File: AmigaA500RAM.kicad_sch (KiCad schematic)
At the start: 0 parts

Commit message: Amiga A500 RAM Schematic
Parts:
- added C1, C2: 1uF, Capacitor_SMD:C_0805_2012Metric, symbol Device:C_Small
- added C10, C11, C12, C13, C14, C3, C4, C5, C6, C7, C8, C9: 0.1uF, Capacitor_SMD:C_0805_2012Metric, symbol Device:C_Small
- added J1: SSQ-128-02-G-D-RA, AmigaA500RAM:PinSocket_2x28_P2.54mm_Horizontal_A501, symbol Connector_Generic:Conn_02x28_Odd_Even
- added JP1: 1MB, Jumper:SolderJumper-2_P1.3mm_Open_RoundedPad1.0x1.5mm, symbol Jumper:SolderJumper_2_Open
- added JP2: CAS 3x or 2x delay, Jumper:SolderJumper-3_P1.3mm_Bridged2Bar12_RoundedPad1.0x1.5mm, symbol Jumper:SolderJumper_3_Bridged12
- added NT1, NT2, NT3, NT4: NetTie_2, NetTie:NetTie-2_SMD_Pad0.5mm, symbol Device:NetTie_2
- added R1, R2, R3: 10K, Resistor_SMD:R_0805_2012Metric, symbol Device:R_Small
- added RN1, RN2, RN3: EXB-2HV680JV, AmigaA500RAM:R_Array08_EXB2H, symbol Device:R_Pack08
- added TP1: TestPoint_Small, AmigaA500RAM:TestPoint_Keystone_5016_Compact, symbol Connector:TestPoint_Small
- added TP2, TP3, TP4, TP5, TP6, TP7: TestPoint_Small, TestPoint:TestPoint_Pad_D1.0mm, symbol Connector:TestPoint_Small
- added U1: 74LVC16T245, Package_SO:TSSOP-48_6.1x12.5mm_P0.5mm, symbol 74xx:74ALVC164245
- added U2: TLV1117LV33, Package_TO_SOT_SMD:SOT-223-3_TabPin2, symbol AmigaA500RAM:TLV1117LV33
- added U3, U4: SN74LVC821A, Package_SO:TSSOP-24_4.4x7.8mm_P0.65mm, symbol AmigaA500RAM:SN74LVC821A
- added U5: SN74LVC244A, Package_SO:TSSOP-20_4.4x6.5mm_P0.65mm, symbol 74xx:74HCT244
- added U6: SN74LVC00A, Package_SO:TSSOP-14_4.4x5mm_P0.65mm, symbol 74xx:74HCT00
- added U7: AS6C6416-55TIN, Package_SO:TSOP-I-48_18.4x12mm_P0.5mm, symbol AmigaA500RAM:AS6C6416
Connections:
- new net: JP2.2 (C), U6.12, U6.13
- new net: RN3.14 (R3.2), U6.2, U6.4, U6.5
- new net: RN3.15 (R2.2), U6.1
- new net: RN1.10 (R7.2), U1.11 (1B6)
- new net: RN1.9 (R8.2), U1.12 (1B7)
- new net: RN2.16 (R1.2), U1.13 (2B0)
- new net: RN2.15 (R2.2), U1.14 (2B1)
- new net: RN2.14 (R3.2), U1.16 (2B2)
- new net: RN2.13 (R4.2), U1.17 (2B3)
- new net: RN2.12 (R5.2), U1.19 (2B4)
- new net: RN1.16 (R1.2), U1.2 (1B0)
- new net: RN2.11 (R6.2), U1.20 (2B5)
- new net: RN2.10 (R7.2), U1.22 (2B6)
- new net: RN2.9 (R8.2), U1.23 (2B7)
- new net: RN1.15 (R2.2), U1.3 (1B1)
- new net: RN1.14 (R3.2), U1.5 (1B2)
- new net: RN1.13 (R4.2), U1.6 (1B3)
- new net: RN1.12 (R5.2), U1.8 (1B4)
- new net: RN1.11 (R6.2), U1.9 (1B5)
- new net +3V3: C10.1, C11.1, C12.1, C13.1, C14.1, C2.1, C6.1, C7.1, C8.1, C9.1, R1.1, R2.1, U1.31 (V_{CC(A)}), U1.42 (V_{CC(A)}), U2.2 (VO), U3.24 (VCC), U4.24 (VCC), U5.20 (VCC), U6.14 (VCC), U7.12 (CE2), U7.37 (VDD), U7.47 (~{BYTE})
- new net +5V: C1.1, C3.1, C4.1, C5.1, J1.1 (Pin_1), J1.2 (Pin_2), J1.51 (Pin_51), J1.52 (Pin_52), U1.18 (V_{CC(B)}), U1.7 (V_{CC(B)}), U2.3 (VI)
- new net A0: U4.14 (Q9), U7.25 (A0)
- new net A1: U4.15 (Q8), U7.24 (A1)
- new net A10: U3.15 (Q8), U7.6 (A10)
- new net A11: U3.16 (Q7), U7.5 (A11)
- new net A12: U3.17 (Q6), U7.4 (A12)
- new net A13: U3.18 (Q5), U7.3 (A13)
- new net A14: U3.19 (Q4), U7.2 (A14)
- new net A15: U3.20 (Q3), U7.1 (A15)
- new net A16: U3.21 (Q2), U7.48 (A16)
- new net A17: U3.22 (Q1), U7.17 (A17)
- new net A18: U3.23 (Q0), U7.16 (A18)
- new net A19: NT1.2, U7.9 (A19)
- new net A2: U4.16 (Q7), U7.23 (A2)
- new net A20: NT2.2, U7.10 (A20)
- new net A21: NT3.2, U7.13 (A21)
- new net A3: U4.17 (Q6), U7.22 (A3)
- new net A4: U4.18 (Q5), U7.21 (A4)
- new net A5: U4.19 (Q4), U7.20 (A5)
- new net A6: U4.20 (Q3), U7.19 (A6)
- new net A7: U4.21 (Q2), U7.18 (A7)
- new net A8: U4.22 (Q1), U7.8 (A8)
- new net A9: U3.14 (Q9), U7.7 (A9)
- new net CAS: TP2.1, U3.13 (Clk), U5.2 (1A0), U6.8
- new net CAS_P1: U5.18 (1Y0), U5.4 (1A1)
- new net CAS_P2: JP2.3 (B), U5.16 (1Y1), U5.6 (1A2)
- new net CAS_P3: JP2.1 (A), U5.14 (1Y2)
- new net GND: C1.2, C10.2, C11.2, C12.2, C13.2, C14.2, C2.2, C3.2, C4.2, C5.2, C6.2, C7.2, C8.2, C9.2, J1.21 (Pin_21), J1.22 (Pin_22), J1.3 (Pin_3), J1.4 (Pin_4), J1.53 (Pin_53), J1.54 (Pin_54), NT1.1, NT2.1, NT3.1, NT4.1, R3.2, TP1.1, U1.10 (GND), U1.15 (GND), U1.21 (GND), U1.28 (GND), U1.34 (GND), U1.39 (GND), U1.4 (GND), U1.45 (GND), U2.1 (GND), U3.1 (OE), U3.12 (GND), U4.1 (OE), U4.12 (GND), U5.1 (1OE), U5.10 (GND), U5.11 (2A3), U5.13 (2A2), U5.19 (2OE), U6.7 (GND), U7.27 (GND), U7.28 (~{OE}), U7.46 (GND)
- new net IO0: U1.26 (2A7), U7.29 (I/O0)
- new net IO1: U1.27 (2A6), U7.31 (I/O1)
- new net IO10: U1.40 (1A5), U7.34 (I/O10)
- new net IO11: U1.41 (1A4), U7.36 (I/O11)
- new net IO12: U1.43 (1A3), U7.39 (I/O12)
- new net IO13: U1.44 (1A2), U7.41 (I/O13)
- new net IO14: U1.46 (1A1), U7.43 (I/O14)
- new net IO15: U1.47 (1A0), U7.45 (I/O15/A19)
- new net IO2: U1.29 (2A5), U7.33 (I/O2)
- new net IO3: U1.30 (2A4), U7.35 (I/O3)
- new net IO4: U1.32 (2A3), U7.38 (I/O4)
- new net IO5: U1.33 (2A2), U7.40 (I/O5)
- new net IO6: U1.35 (2A1), U7.42 (I/O6)
- new net IO7: U1.36 (2A0), U7.44 (I/O7)
- new net IO8: U1.37 (1A7), U7.30 (I/O8)
- new net IO9: U1.38 (1A6), U7.32 (I/O9)
- new net IO_DIR: R1.2, TP6.1, U1.1 (1DIR), U1.24 (2DIR), U4.23 (Q0)
- new net RAS: TP3.1, U4.13 (Clk), U6.3
- new net RAS1: JP1.1 (A), TP4.1, U6.6
- new net SEL_A18: JP1.2 (B), R3.1, U3.2 (D0)
- new net XDRA0: J1.23 (Pin_23), U3.11 (D9), U4.11 (D9)
- new net XDRA1: J1.24 (Pin_24), U3.10 (D8), U4.10 (D8)
- new net XDRA2: J1.25 (Pin_25), U3.9 (D7), U4.9 (D7)
- new net XDRA3: J1.26 (Pin_26), U3.8 (D6), U4.8 (D6)
- new net XDRA4: J1.27 (Pin_27), U3.7 (D5), U4.7 (D5)
- new net XDRA5: J1.28 (Pin_28), U3.6 (D4), U4.6 (D4)
- new net XDRA6: J1.29 (Pin_29), U3.5 (D3), U4.5 (D3)
- new net XDRA7: J1.30 (Pin_30), U3.4 (D2), U4.4 (D2)
- new net XDRA8: J1.31 (Pin_31), U3.3 (D1), U4.3 (D1)
- new net XDRD0: J1.5 (Pin_5), RN2.8 (R8.1)
- new net XDRD1: J1.6 (Pin_6), RN2.7 (R7.1)
- new net XDRD10: J1.15 (Pin_15), RN1.6 (R6.1)
- new net XDRD11: J1.16 (Pin_16), RN1.5 (R5.1)
- new net XDRD12: J1.17 (Pin_17), RN1.4 (R4.1)
- new net XDRD13: J1.18 (Pin_18), RN1.3 (R3.1)
- new net XDRD14: J1.19 (Pin_19), RN1.2 (R2.1)
- new net XDRD15: J1.20 (Pin_20), RN1.1 (R1.1)
- new net XDRD2: J1.7 (Pin_7), RN2.6 (R6.1)
- new net XDRD3: J1.8 (Pin_8), RN2.5 (R5.1)
- new net XDRD4: J1.9 (Pin_9), RN2.4 (R4.1)
- new net XDRD5: J1.10 (Pin_10), RN2.3 (R3.1)
- new net XDRD6: J1.11 (Pin_11), RN2.2 (R2.1)
- new net XDRD7: J1.12 (Pin_12), RN2.1 (R1.1)
- new net XDRD8: J1.13 (Pin_13), RN1.8 (R8.1)
- new net XDRD9: J1.14 (Pin_14), RN1.7 (R7.1)
- new net ~{CASL}: RN3.12 (R5.2), U5.17 (2A0), U6.10
- new net ~{CASU}: RN3.13 (R4.2), U5.15 (2A1), U6.9
- new net ~{EXRAM}: J1.32 (Pin_32), NT4.2
- new net ~{IO_BHE}: U5.5 (2Y1), U7.14 (~{BHE})
- new net ~{IO_BLE}: U5.3 (2Y0), U7.15 (~{BLE})
- new net ~{IO_OE}: R2.2, TP7.1, U1.25 (2~{OE}), U1.48 (1~{OE}), U6.11, U7.26 (~{CE1})
- new net ~{IO_WE}: U5.12 (1Y3), U7.11 (~{WE})
- new net ~{WE}: RN3.16 (R1.2), TP5.1, U4.2 (D0), U5.8 (1A3)
- new net ~{XCASL}: J1.35 (Pin_35), RN3.5 (R5.1)
- new net ~{XCASU}: J1.36 (Pin_36), RN3.4 (R4.1)
- new net ~{XOE}: J1.34 (Pin_34), RN3.6 (R6.1)
- new net ~{XRAS0}: J1.38 (Pin_38), RN3.2 (R2.1)
- new net ~{XRAS1}: J1.37 (Pin_37), RN3.3 (R3.1)
- new net ~{XWE}: J1.39 (Pin_39), RN3.1 (R1.1)
- no-connect marks 0 -> 21
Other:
- note added: "+12V"
- note added: "-12V"
- note added: "CLK: L->H"
- note added: "L: B->A H: B<-A"
- note added: "Note: Assume ~{XOE} tied to GND, otherwise move RAS1 as ~{RAS1} through spare '244 for ~{A18} and invert ~{XOE} for XOE as input for ~{IO_OE} ?"
- note added: "Note: CLK + ~8ns t_{pd} for A[*]"
- note added: "Note: Latch ~{XWE} as IO_DIR to ~{CAS} (~{IO_OE}) L->H"
- note added: "Note: Timing diagrams U10/U12 P1 (OE) is ~{OEB} for write when L U11/U13 P1 ~{OC} is ~{OEL} U11/U13 P11 ~{C} is ~{LATCH} for read on H->L"
- note added: "Note: ~4ns t_{pd}"
- note added: "XA2"
- note added: "XA3"
- note added: "XA4"
- note added: "XA5"
- note added: "XD0"
- note added: "XD1"
- note added: "XD2"
- note added: "XD3"
- note added: "~{CCK_A}"
- note added: "~{RAS0}"
- note added: "~{RAS1}"
- note added: "~{XCLKCS}"
- note added: "~{XCLKRD}"
- note added: "~{XCLKWR}"

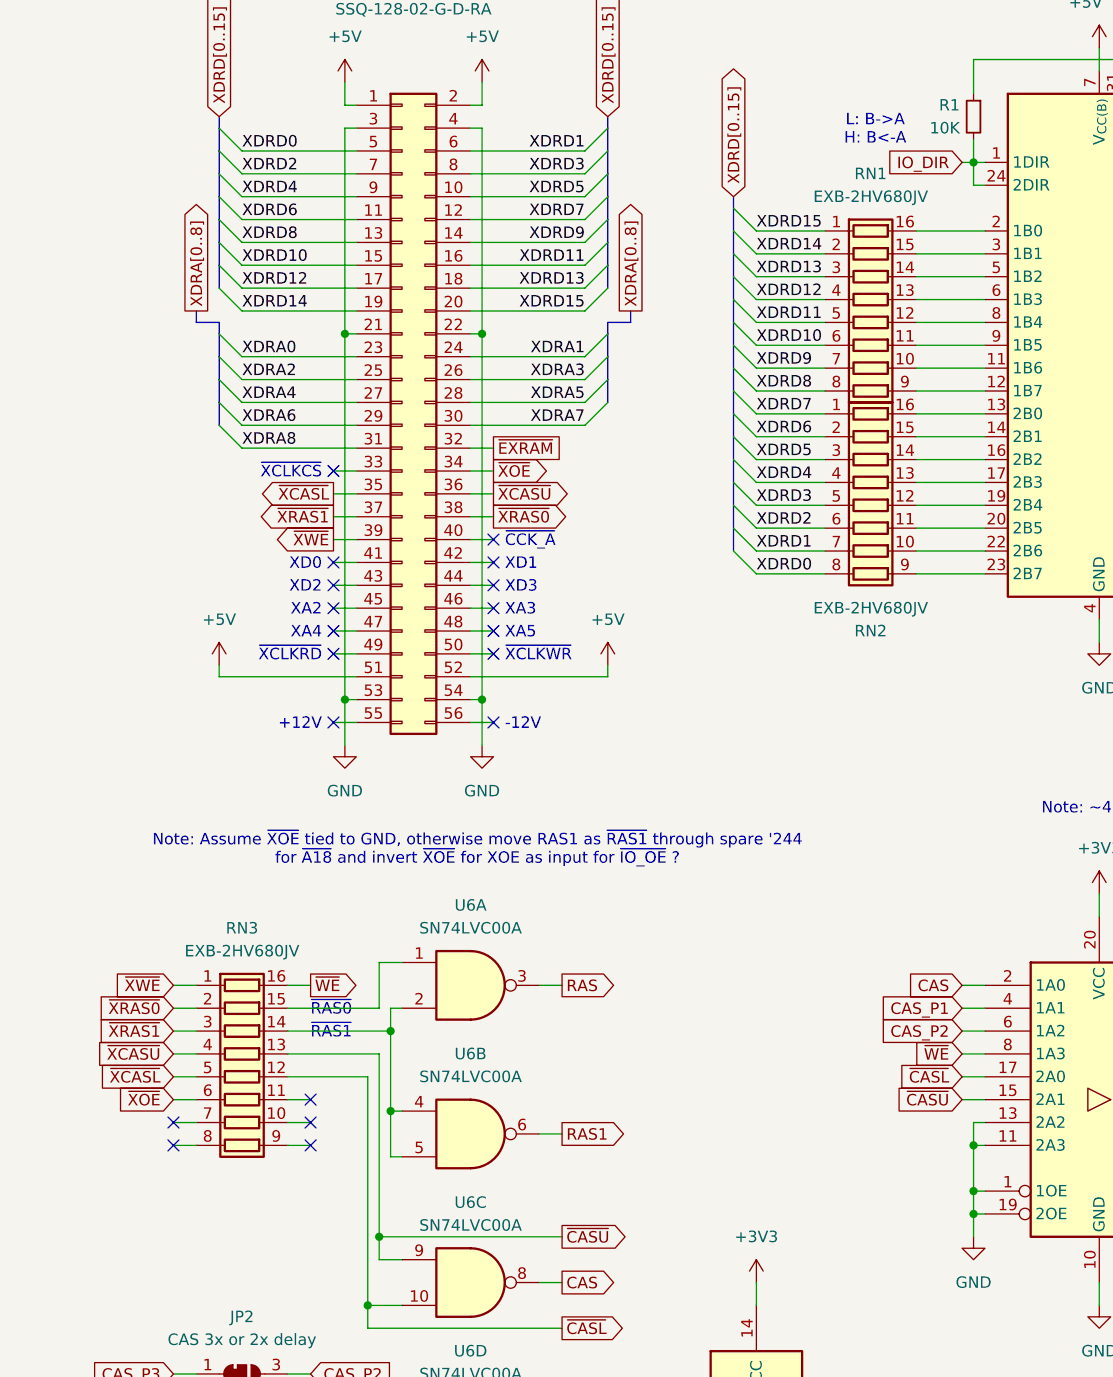
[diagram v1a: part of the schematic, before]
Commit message: Update resistor arrays to 4x0603
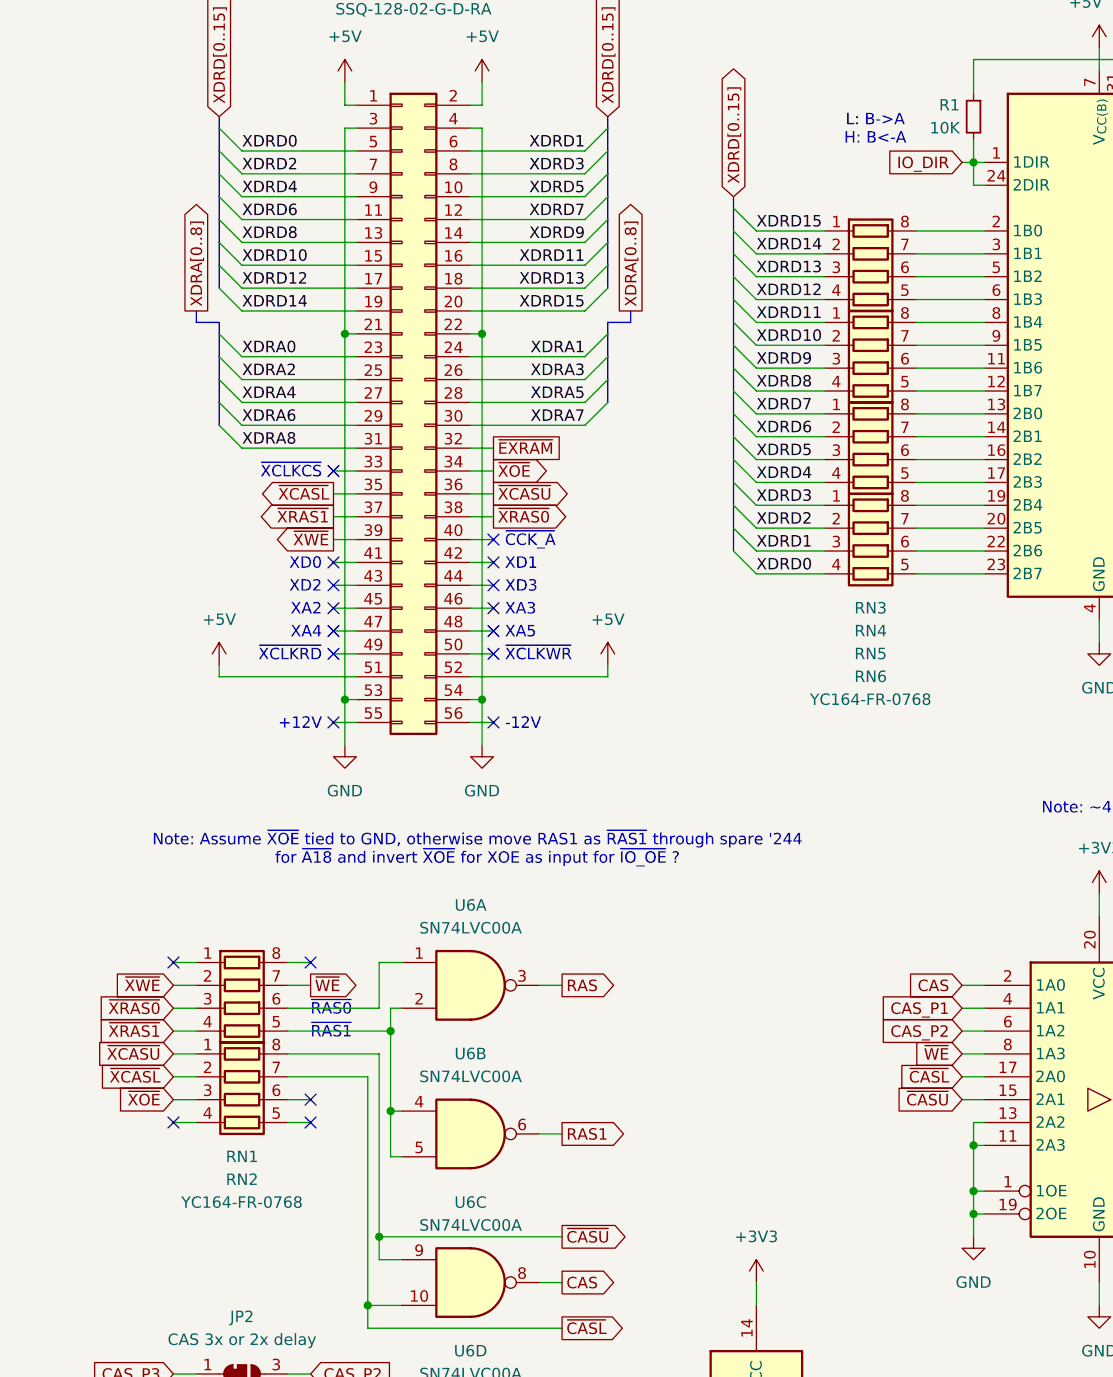
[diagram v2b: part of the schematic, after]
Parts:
- removed RN1, RN2, RN3: EXB-2HV680JV, AmigaA500RAM:R_Array08_EXB2H, symbol Device:R_Pack08
- added RN1, RN2, RN3, RN4, RN5, RN6: YC164-FR-0768, Resistor_SMD:R_Array_Convex_4x0603, symbol Device:R_Pack04
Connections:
- net XDRD0: now also RN6.4 (R4.1)
- net XDRD1: now also RN6.3 (R3.1)
- net XDRD10: now also RN4.2 (R2.1)
- net XDRD11: now also RN4.1 (R1.1)
- net XDRD12: now also RN3.4 (R4.1)
- net XDRD13: now also RN3.3 (R3.1)
- net XDRD14: now also RN3.2 (R2.1)
- net XDRD15: now also RN3.1 (R1.1)
- net XDRD2: now also RN6.2 (R2.1)
- net XDRD3: now also RN6.1 (R1.1)
- net XDRD4: now also RN5.4 (R4.1)
- net XDRD5: now also RN5.3 (R3.1)
- net XDRD6: now also RN5.2 (R2.1)
- net XDRD7: now also RN5.1 (R1.1)
- net XDRD8: now also RN4.4 (R4.1)
- net XDRD9: now also RN4.3 (R3.1)
- net ~{CASL}: now also RN2.7 (R2.2)
- net ~{CASU}: now also RN2.8 (R1.2)
- net ~{WE}: now also RN1.7 (R2.2)
- net ~{XCASL}: now also RN2.2 (R2.1)
- net ~{XCASU}: now also RN2.1 (R1.1)
- net ~{XOE}: now also RN2.3 (R3.1)
- net ~{XRAS0}: now also RN1.3 (R3.1)
- net ~{XRAS1}: now also RN1.4 (R4.1)
- net ~{XWE}: now also RN1.2 (R2.1)
- net at U6.2, U6.4, U6.5: now also RN1.5 (R4.2)
- net at U6.1: now also RN1.6 (R3.2)
- net at U1.11 (1B6): now also RN4.6 (R3.2)
- net at U1.12 (1B7): now also RN4.5 (R4.2)
- net at U1.13 (2B0): now also RN5.8 (R1.2)
- net at U1.14 (2B1): now also RN5.7 (R2.2)
- net at U1.16 (2B2): now also RN5.6 (R3.2)
- net at U1.17 (2B3): now also RN5.5 (R4.2)
- net at U1.19 (2B4): now also RN6.8 (R1.2)
- net at U1.2 (1B0): now also RN3.8 (R1.2)
- net at U1.20 (2B5): now also RN6.7 (R2.2)
- net at U1.22 (2B6): now also RN6.6 (R3.2)
- net at U1.23 (2B7): now also RN6.5 (R4.2)
- net at U1.3 (1B1): now also RN3.7 (R2.2)
- net at U1.5 (1B2): now also RN3.6 (R3.2)
- net at U1.6 (1B3): now also RN3.5 (R4.2)
- net at U1.8 (1B4): now also RN4.8 (R1.2)
- net at U1.9 (1B5): now also RN4.7 (R2.2)
